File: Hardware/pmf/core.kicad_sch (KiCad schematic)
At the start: 39 parts, among them U1 AS3320, U2 TL072

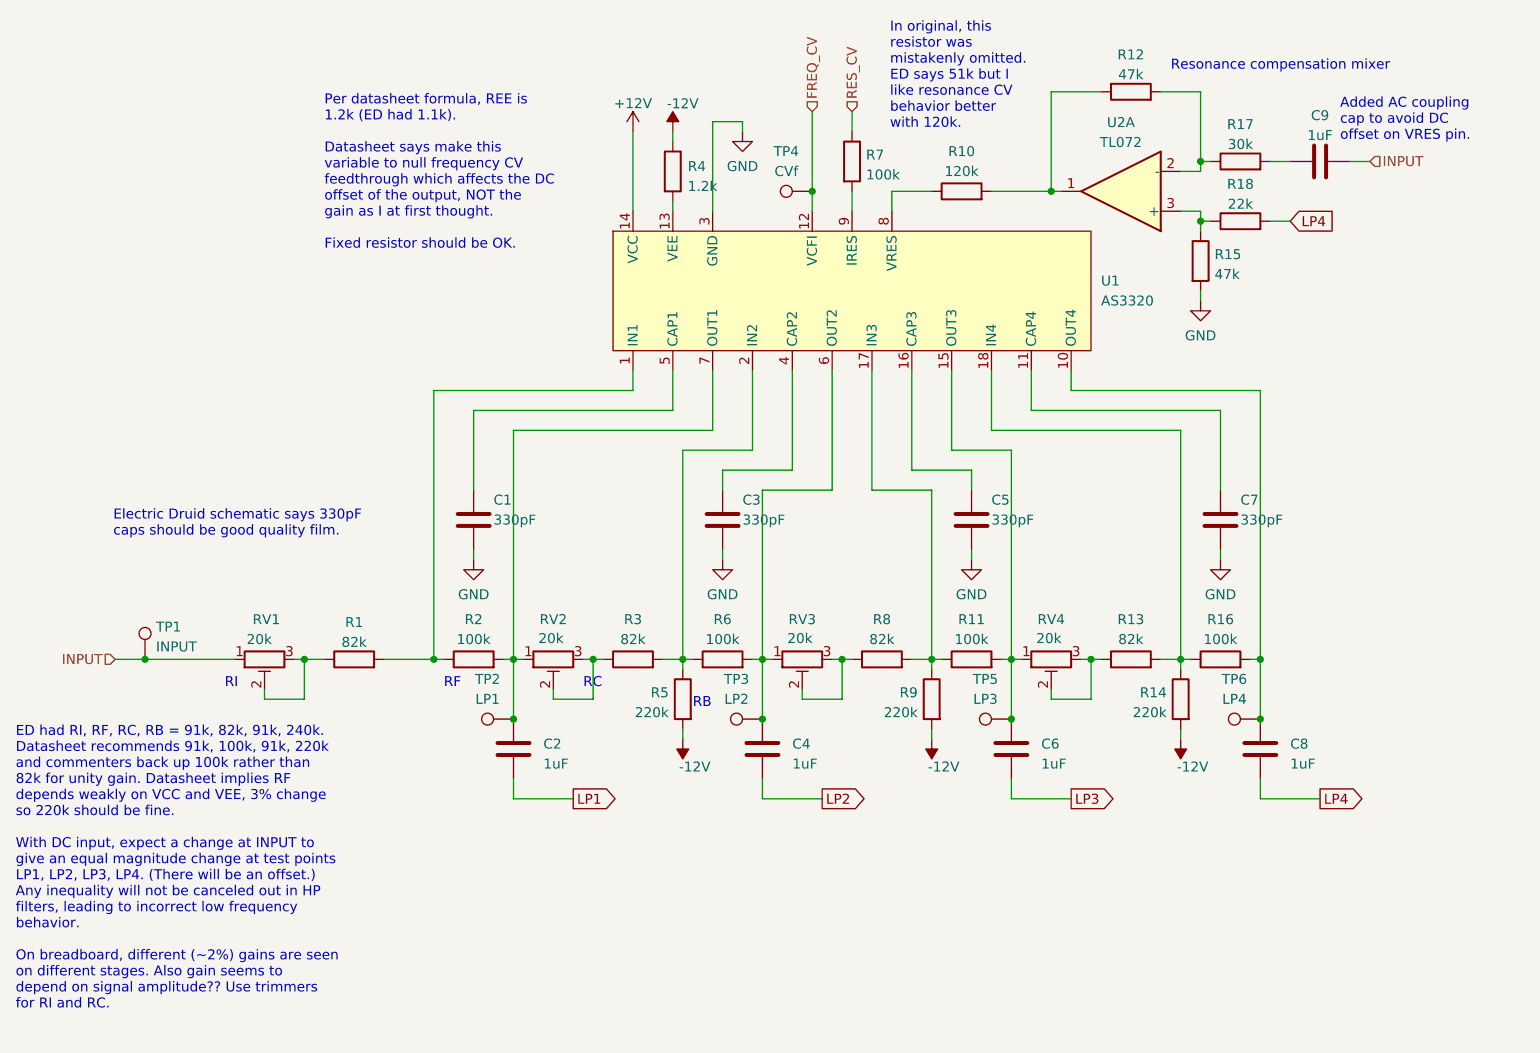
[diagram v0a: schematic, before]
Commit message: Global labels to heir, fixing input bug; buffer LP1-4; more clearance for rot switch
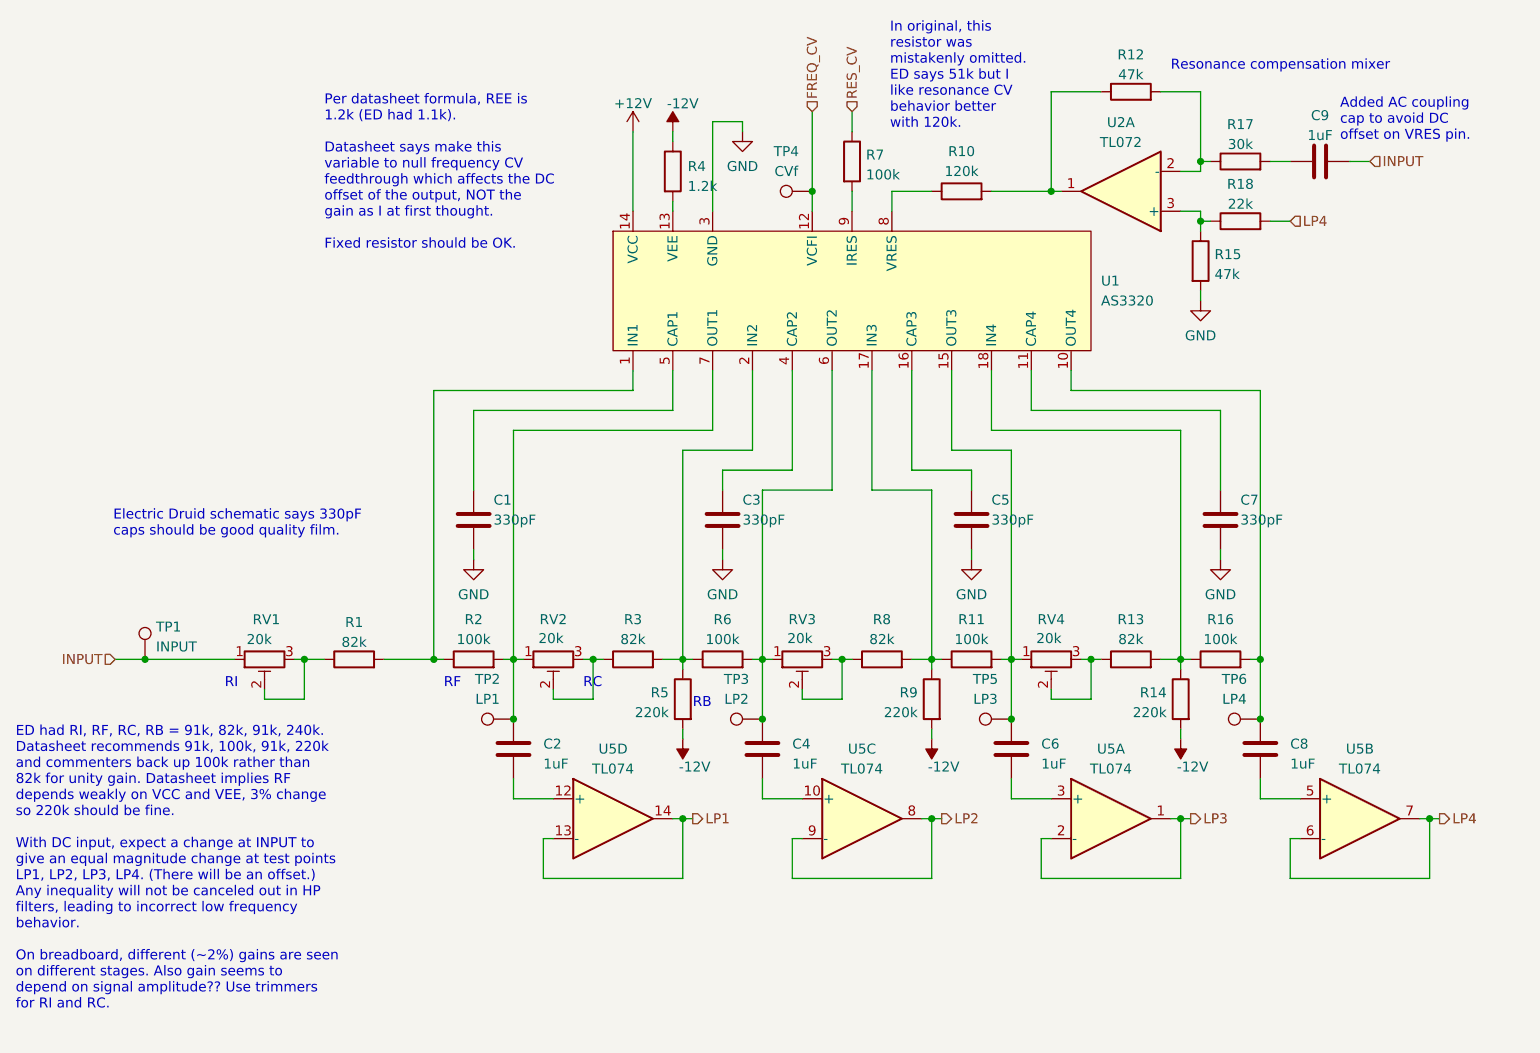
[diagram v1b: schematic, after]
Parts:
- added U5: TL074, AO_tht:DIP-14_W7.62mm_Socket_LongPads, symbol AO_symbols:TL074
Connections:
- net LP1: now also U5.13 (-), U5.14; no longer C2.2
- net LP2: now also U5.8, U5.9 (-); no longer C4.2
- net LP3: now also U5.1, U5.2 (-); no longer C6.2
- net LP4: now also U5.6 (-), U5.7; no longer C8.2
- new net: C8.2, U5.5 (+)
- new net: C2.2, U5.12 (+)
- new net: C6.2, U5.3 (+)
- new net: C4.2, U5.10 (+)

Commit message: Docs; add bias current resistors
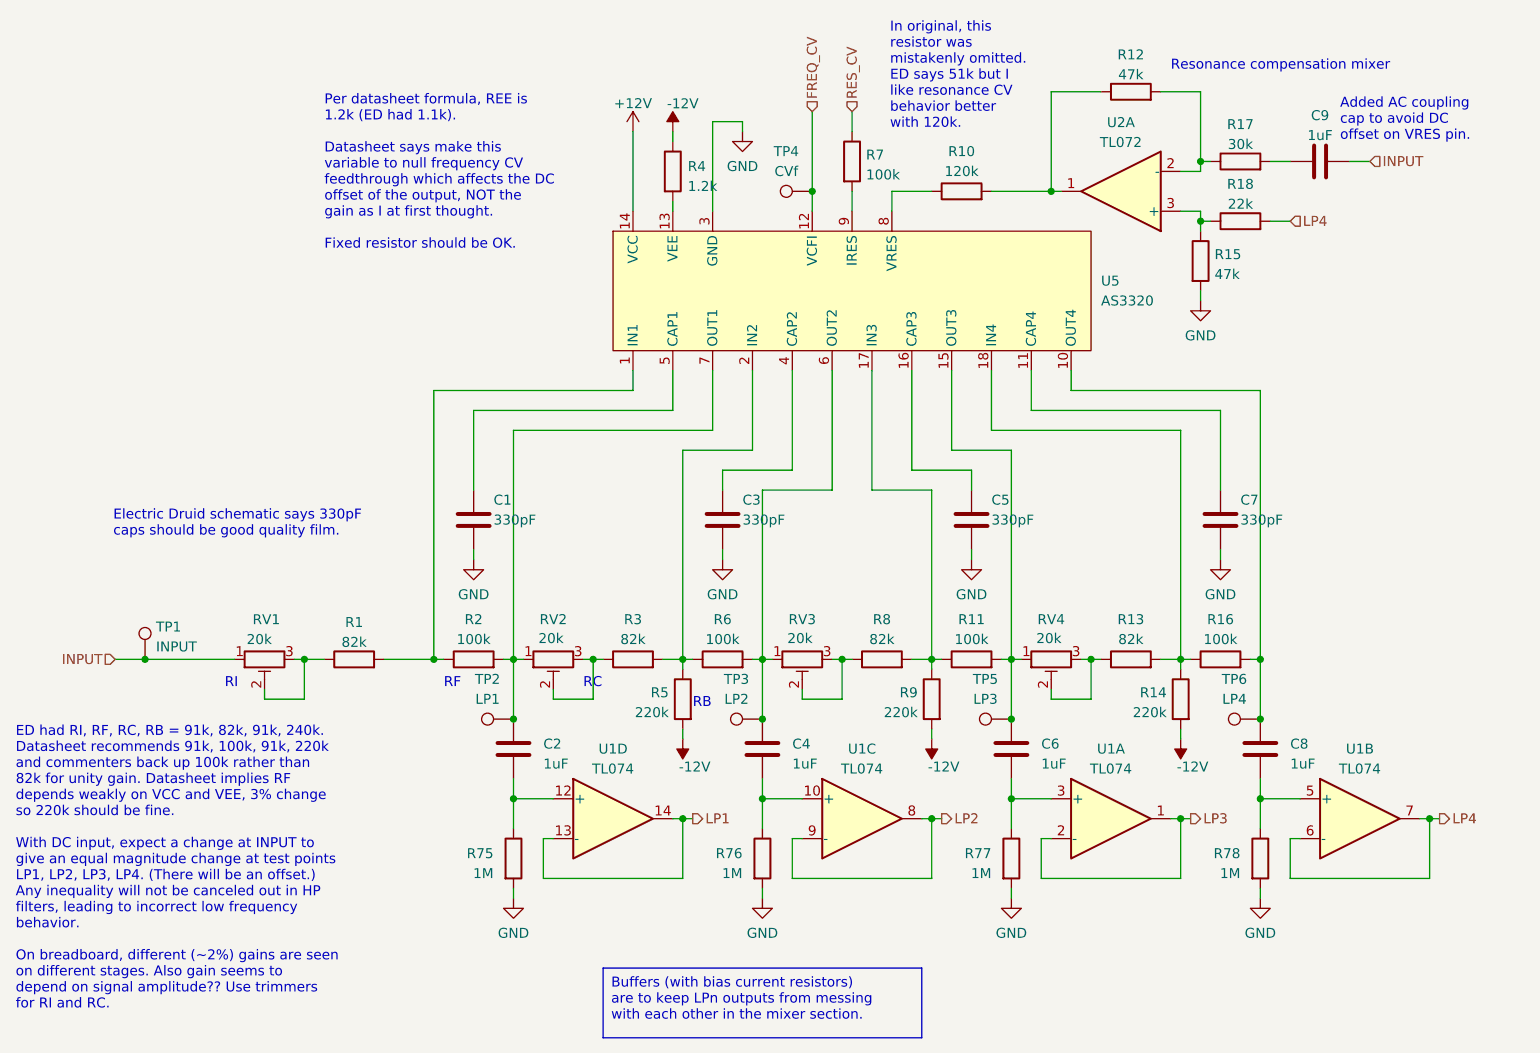
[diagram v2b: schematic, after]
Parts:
- added R75, R76, R77, R78: 1M, AO_tht:R_Axial_DIN0207_L6.3mm_D2.5mm_P2.54mm_Vertical, symbol AO_symbols:R
- renumbered U5 to U1, U1 to U5
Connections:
- net GND: now also R75.2, R76.2, R77.2, R78.2
- net at C8.2, U1.5 (+): now also R78.1
- net at C2.2, U1.12 (+): now also R75.1
- net at C6.2, U1.3 (+): now also R77.1
- net at C4.2, U1.10 (+): now also R76.1
